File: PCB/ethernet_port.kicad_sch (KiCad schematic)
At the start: 60 parts, among them IC10 MMBT3904-AQ, IC11 MMBT3904-AQ, IC5 W5500, IC6 CP2102N-A02-GQFN24, IC7 USBLC6-2SC6, J1 USB_C_Receptacle_USB2.0_16P, J2 TMJ0026ABNL, Y3 ASE-25.000MHZ-LC-T

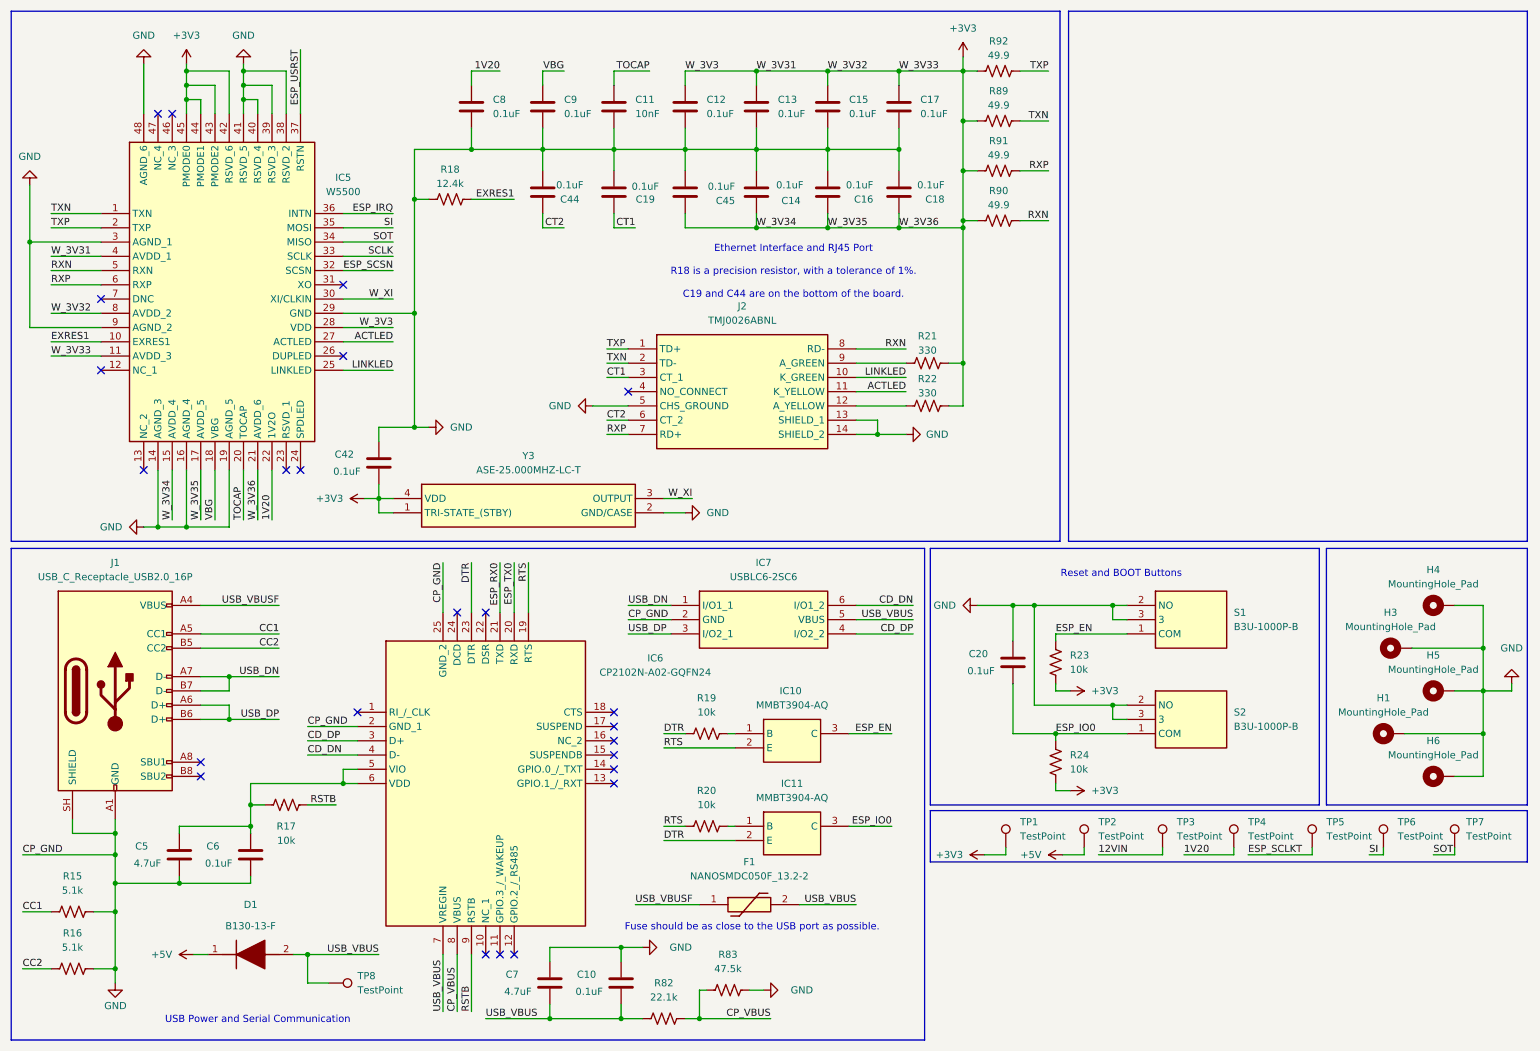
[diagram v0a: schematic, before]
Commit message: Board Modifications and Initial Comms w/ Sensors
Modified wiring to separate ethernet reset from SC16 reset, adjusted pinouts and power, worked on code to get board talking to sensors. Ethernet still needs a bodge wire at this point.
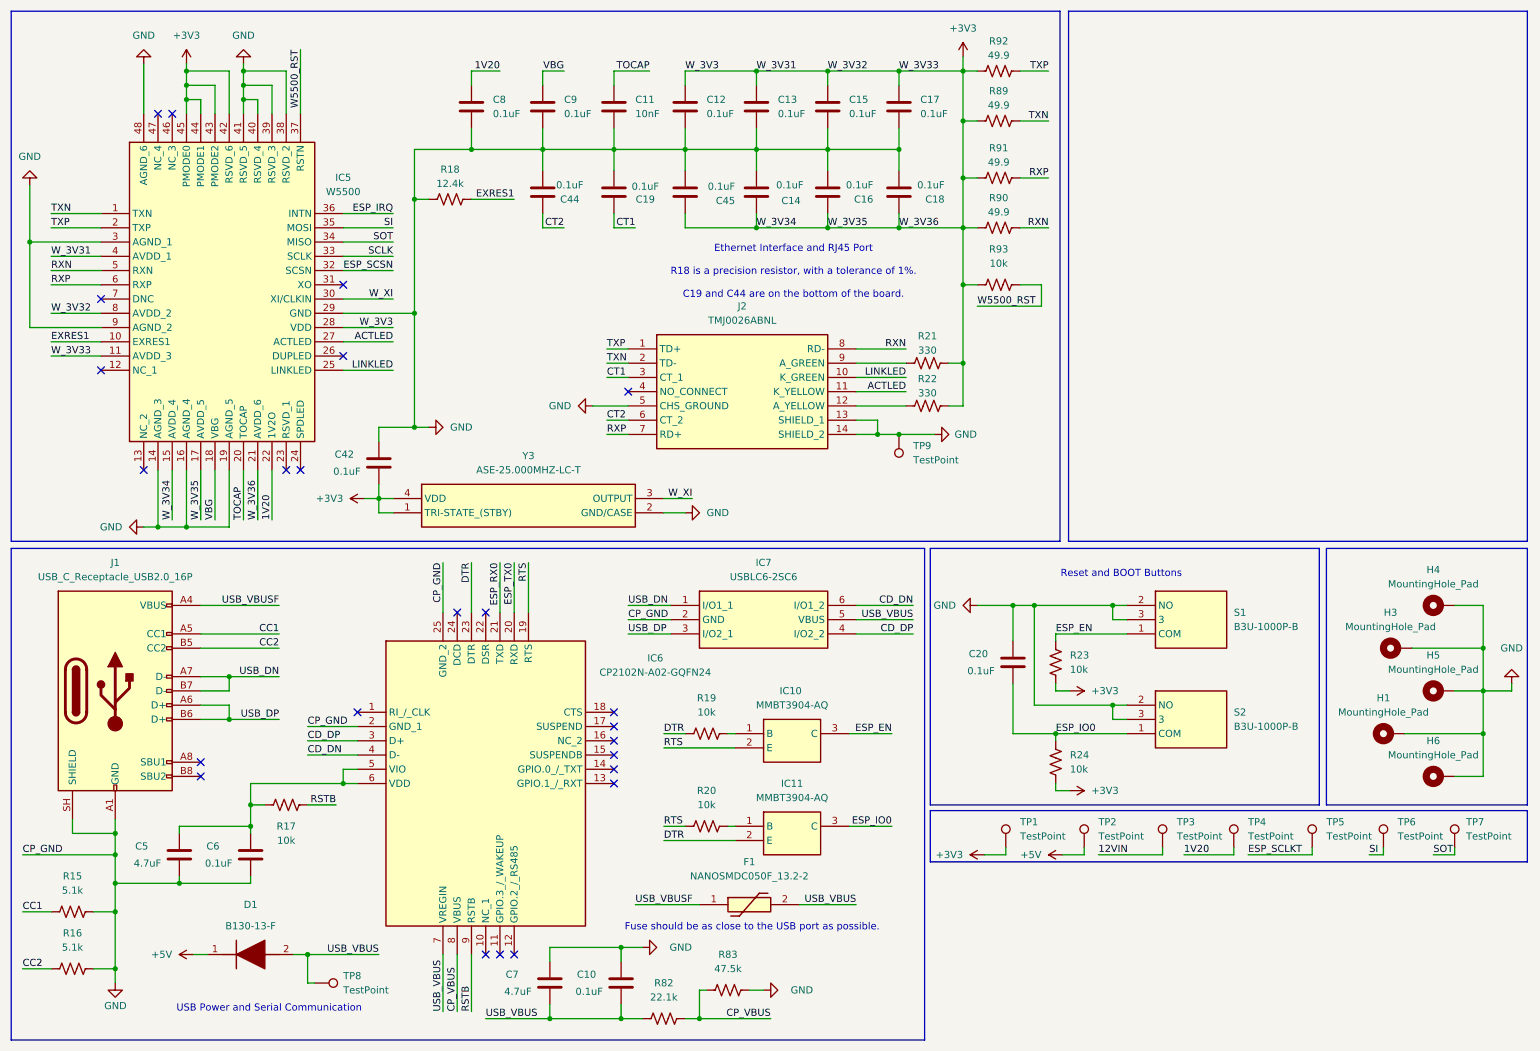
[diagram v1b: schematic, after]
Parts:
- added R93: 10k, Resistor_SMD:R_0805_2012Metric_Pad1.20x1.40mm_HandSolder, symbol Device:R_US
- added TP9: TestPoint, TestPoint:TestPoint_Pad_D3.0mm, symbol Connector:TestPoint
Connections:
- net +3V3: now also R93.1
- net GND: now also TP9.1
- net ESP_USRST renamed W5500_RST
- net W5500_RST: now also R93.2
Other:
- moved on the sheet: R90, R91, TP8

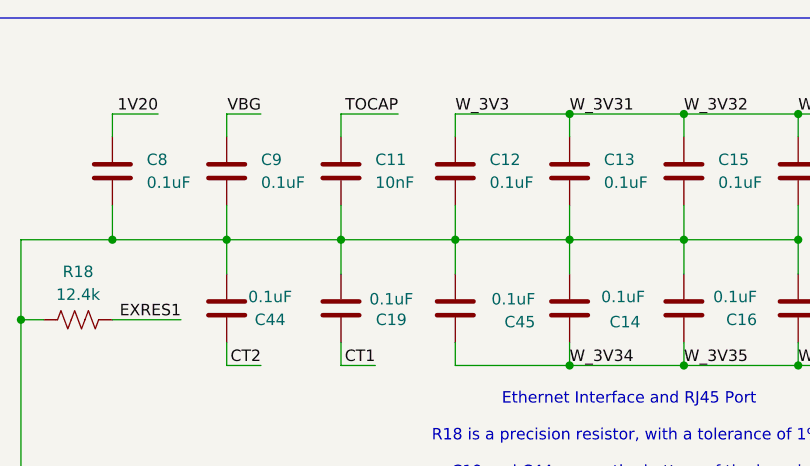
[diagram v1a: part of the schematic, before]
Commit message: Adjust PCB layout and update capacitor value
Fix IC5 (W5500) reference rotation from 180° to 0°. Reposition C8 capacitor and reorganize W5500_RST routing traces. Update ethernet port capacitor value from 10nF to 4.7uF.
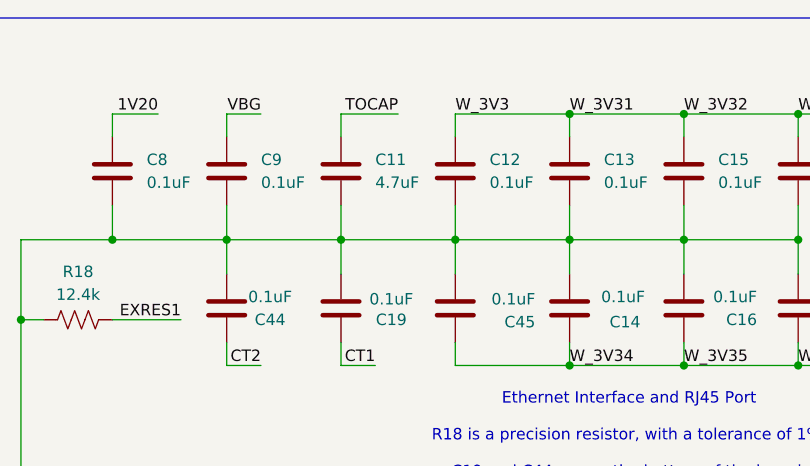
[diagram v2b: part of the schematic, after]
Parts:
- C11: value 10nF -> 4.7uF
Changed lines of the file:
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@@
 			)
 		)
-		(property "Value" "10nF"
+		(property "Value" "4.7uF"
 			(at 124.46 31.7499 0)
 			(show_name no)

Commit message: The W5500 actually works, I just wired it wrong
Pulled back some pins and it's working now! Fixed this error in schematic, code was updated to reflect this
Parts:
- removed C9: 0.1uF, Capacitor_SMD:C_0805_2012Metric_Pad1.18x1.45mm_HandSolder, symbol Device:C
- added TP10: TestPoint, TestPoint:TestPoint_Pad_D3.0mm, symbol Connector:TestPoint
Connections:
- net +3V3: no longer IC5.42 (RSVD_6)
- net ESP_SCSN: now also TP10.1
- net GND: now also IC5.23 (RSVD_1); no longer IC5.38 (RSVD_2), IC5.39 (RSVD_3), IC5.40 (RSVD_4), IC5.41 (RSVD_5)
- net VBG: no longer names the net of IC5.18 (VBG)
- no-connect marks 24 -> 29
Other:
- moved on the sheet: C8
